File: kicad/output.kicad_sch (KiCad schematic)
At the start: 17 parts, among them SW1 BYPASS, U2 NE5532, U5 NE5532

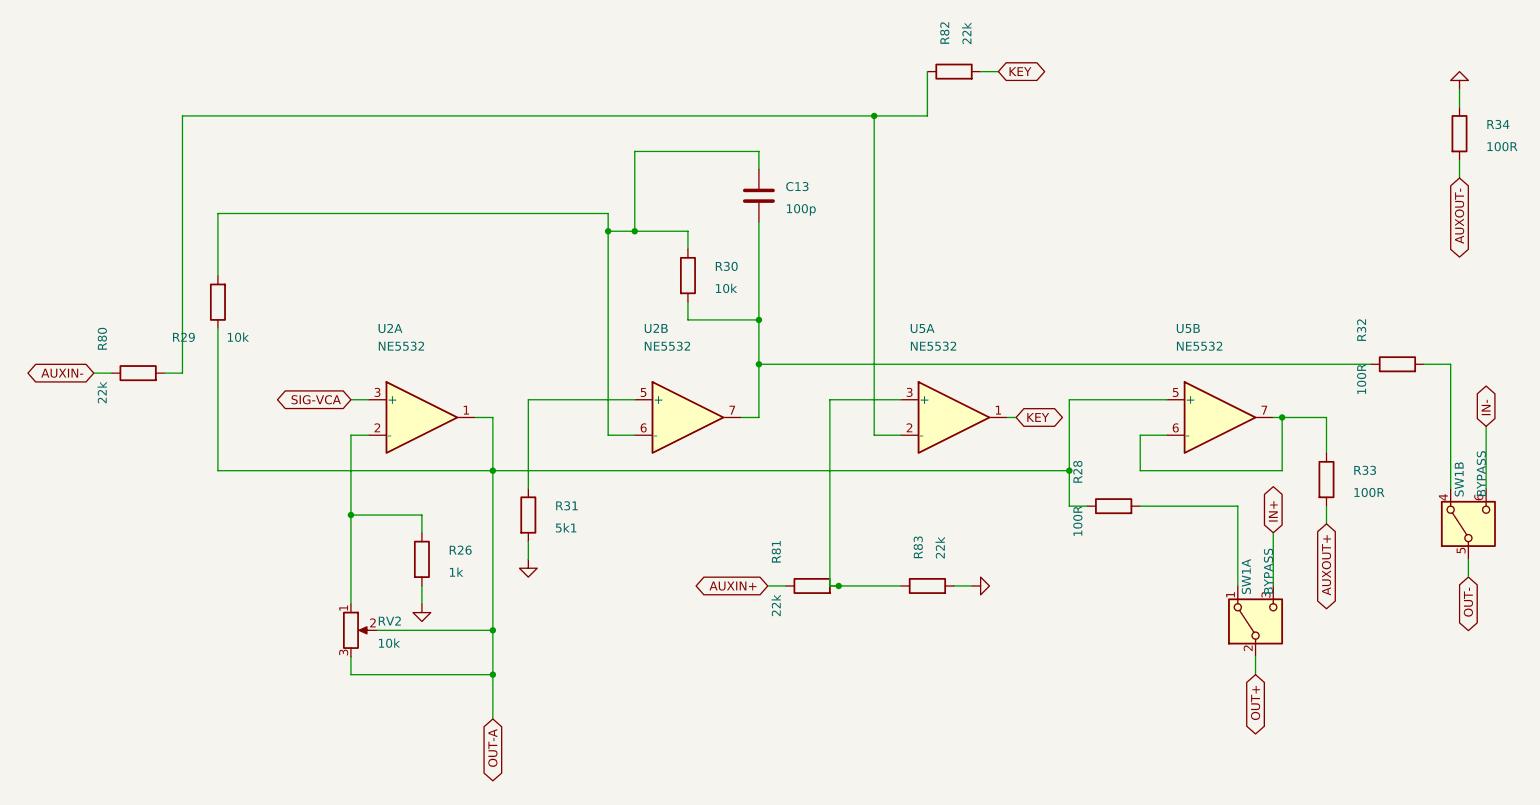
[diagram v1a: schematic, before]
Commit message: Add reorganised schematic to split files.
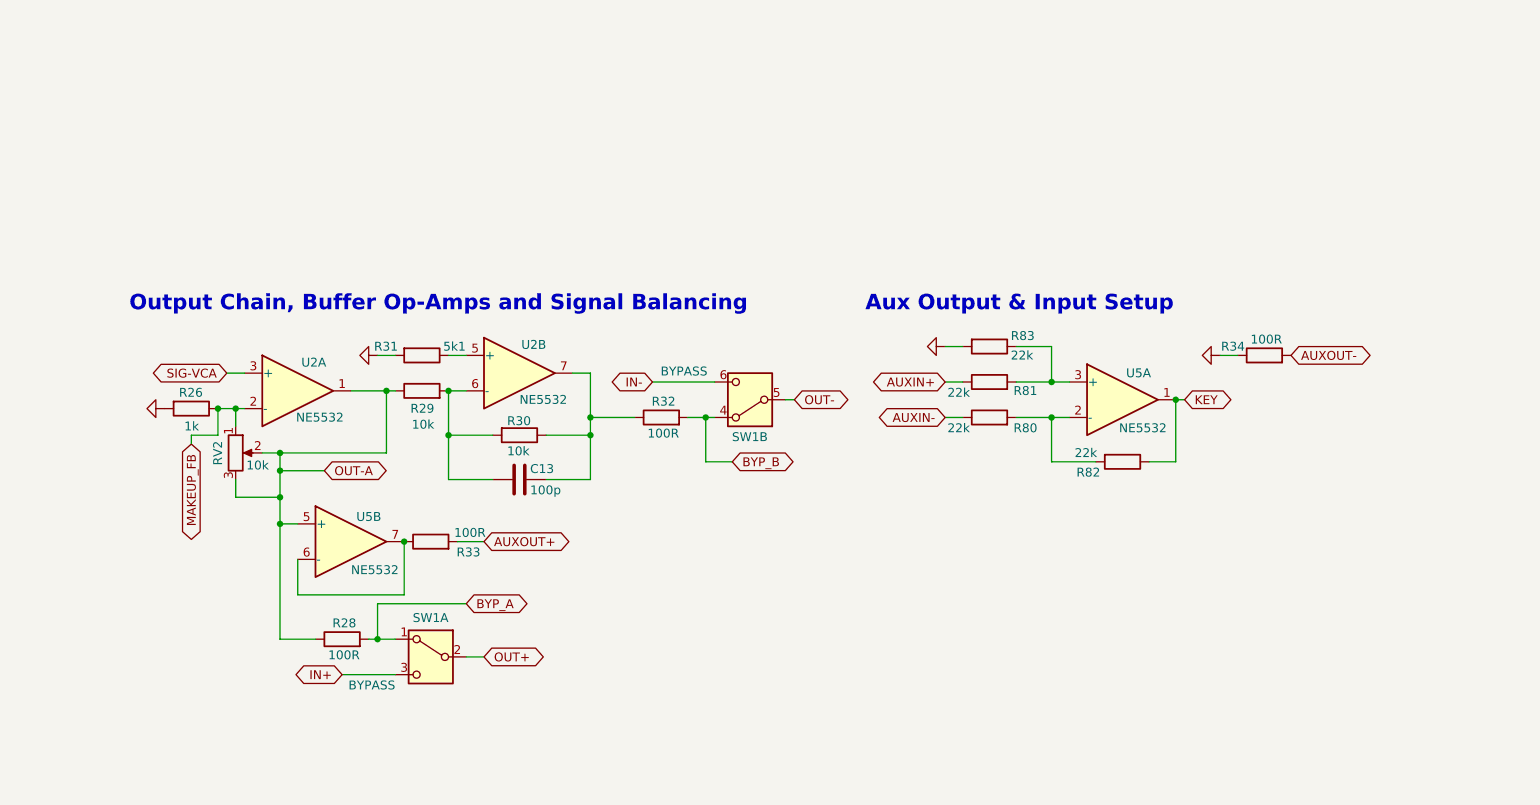
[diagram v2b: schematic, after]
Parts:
- RV2: now left out of the parts list
- SW1: footprint (none) -> Connector_PinHeader_2.54mm:PinHeader_1x06_P2.54mm_Vertical; now left out of the parts list
- U2, U5: footprint Package_DIP:DIP-8_W7.62mm -> Package_DIP:DIP-8_W7.62mm_Socket
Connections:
- net KEY: now also R82.1; no longer R82.2
- net at C13.1, R30.1: now also R32.1, U2.7; no longer R29.2, U2.6 (-)
- net at C13.2, R30.2: now also R29.2, U2.6 (-); no longer R32.1, U2.7
- net BYP_A: now reaches R28.2, SW1.1 (A)
- net MAKEUP_FB: now reaches R26.1, RV2.1, U2.2 (-)
- net at R80.2, U5.2 (-): now also R82.2; no longer R82.1
- net BYP_B: now reaches R32.2, SW1.4 (A)
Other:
- note added: "Aux Output & Input Setup"
- note added: "Output Chain, Buffer Op-Amps and Signal Balancing"
